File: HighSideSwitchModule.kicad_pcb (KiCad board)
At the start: 2 copper layers, 44.5 x 44.5 mm, 31 parts, among them J1 M3, J2 M3, J3 M3, J4 M3, J5 Input, J6 VOUT, J7 VIn, Q3 Q_PMOS_GSD, Q5 Q_NMOS_GDS, U3 IRS2075

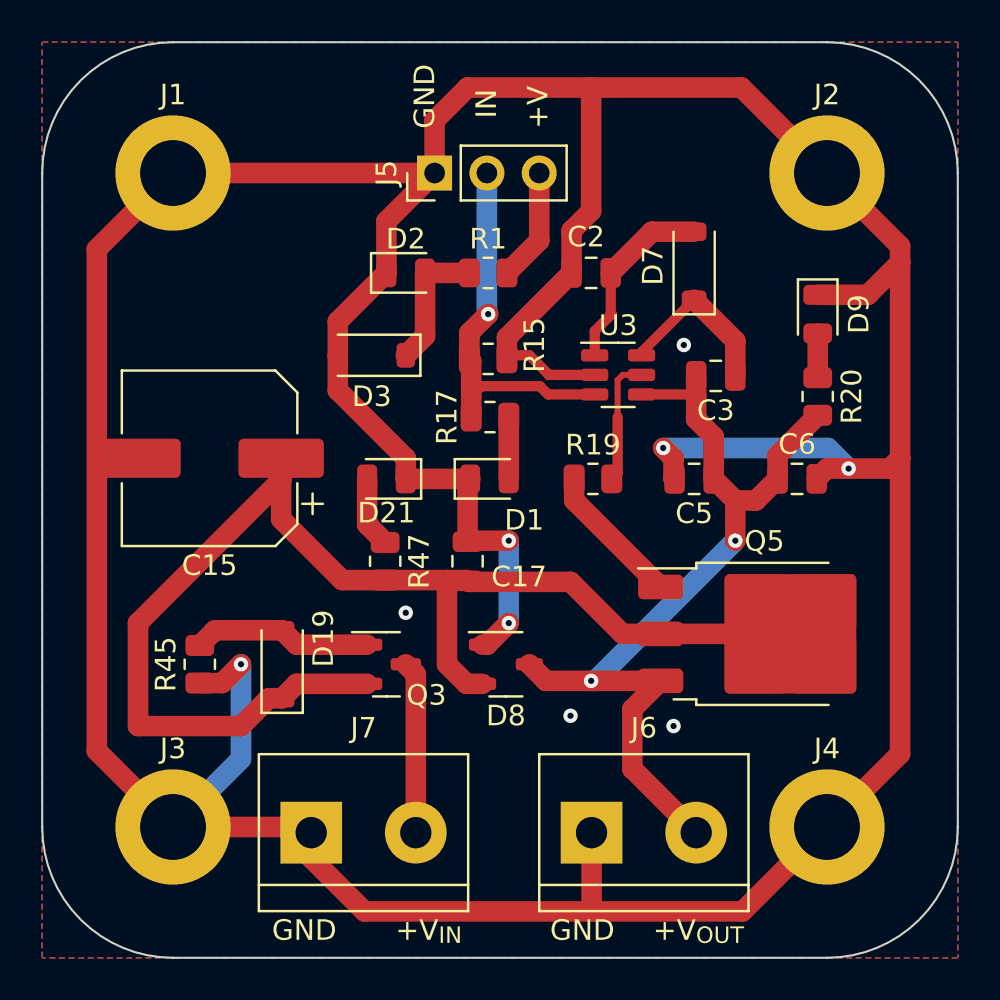
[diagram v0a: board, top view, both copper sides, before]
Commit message: Fixed FETs on input.
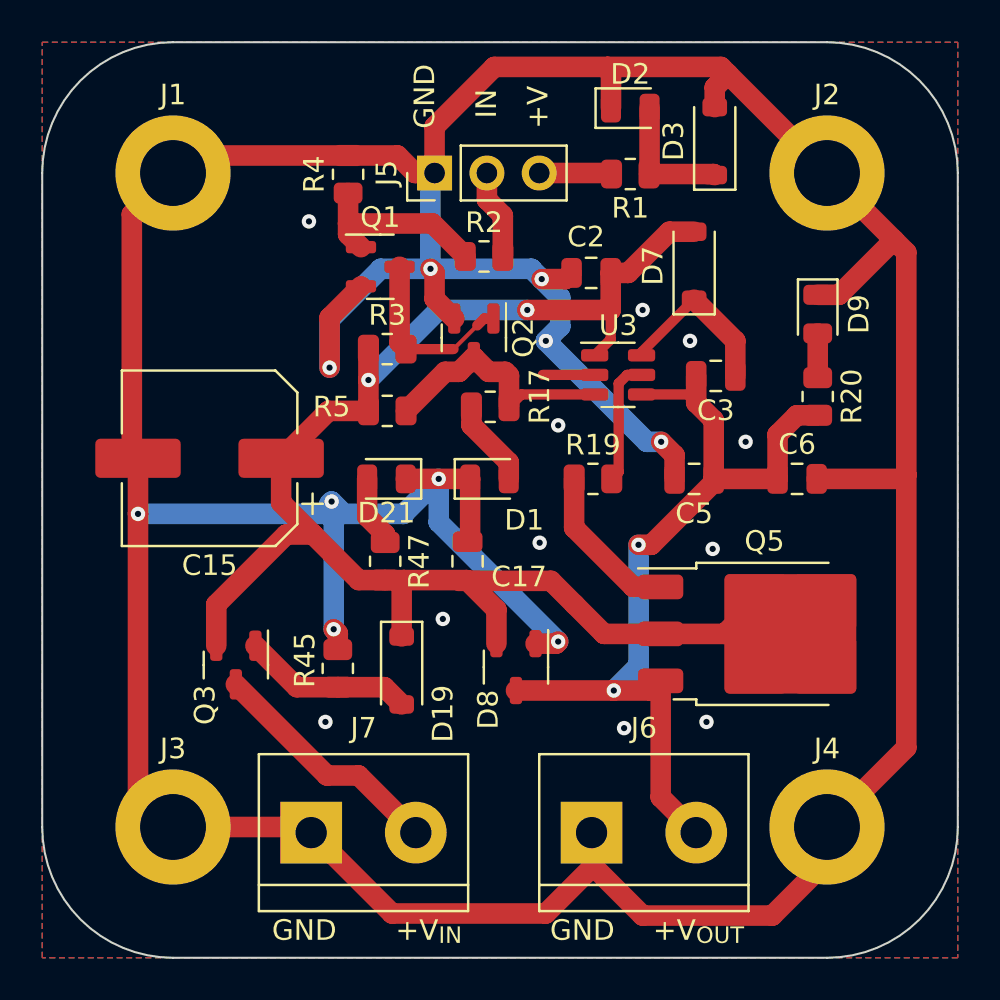
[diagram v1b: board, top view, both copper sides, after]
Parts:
- removed R15: 10kΩ, Resistor_SMD:R_0805_2012Metric
- added Q1: Q_NMOS_GSD, Package_TO_SOT_SMD:SOT-23, F.Cu at (149.8, 61.7)
- added Q2: Q_NMOS_GSD, Package_TO_SOT_SMD:SOT-23, F.Cu at (154.3, 65.2)
- added R2: 1kΩ, Resistor_SMD:R_0805_2012Metric, F.Cu at (154.8, 61.2)
- added R3: 10kΩ, Resistor_SMD:R_0805_2012Metric, F.Cu at (150.1, 65.7)
- added R4: 100kΩ, Resistor_SMD:R_0805_2012Metric, F.Cu at (148.2, 57.2)
- added R5: 10kΩ, Resistor_SMD:R_0805_2012Metric, F.Cu at (150.1, 68.7)
- moved D3 19.6 mm to (166.0, 55.6), turned to 90 degrees
- moved D2 13.5 mm to (161.9, 54.0)
- moved R1 8.41 mm to (161.9, 57.2), turned to 180 degrees
- moved Q3 7.31 mm to (142.8, 81.0), turned to -90 degrees
- moved R45 6.70 mm to (147.7, 81.2), turned to -90 degrees
- moved D19 5.81 mm to (150.8, 81.3), turned to -90 degrees
- moved D8 0.51 mm to (156.3, 81.1), turned to -90 degrees
- moved R17 0.50 mm to (155.1, 68.5), turned to 0 degrees
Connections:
- C2 pad 1: Net-(D7-A) -> +12V
- D7 pad 2: Net-(D7-A) -> +12V
- R17 pad 2: /HighSideGate/IN -> Net-(Q2-D)
- U3 pad 1: Net-(D7-A) -> +12V
- U3 pad 3: /HighSideGate/IN -> Net-(Q2-D)
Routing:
- net GND: track 229.5 -> 245.0 mm, vias 9 -> 21
- net /HighSideGate/IN: track 18.7 -> 4.37 mm, vias 1 -> 0
- net Net-(Q2-D): track 0.00 -> 12.4 mm
- net +12V: track 64.0 -> 73.6 mm, vias 0 -> 2
- net Net-(D7-A): track 9.24 -> 0.00 mm
- net Net-(Q1-G): track 0.00 -> 9.24 mm
- net Net-(Q1-D): track 0.00 -> 8.99 mm
- net Net-(J7-Pin_2): track 8.38 -> 11.7 mm
- net Net-(J5-Pin_3): track 5.50 -> 3.53 mm
- net Net-(D1-A): track 3.00 -> 4.25 mm
- net Net-(Q5-G): track 6.98 -> 7.76 mm
